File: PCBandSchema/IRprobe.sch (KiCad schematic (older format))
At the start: 16 parts, among them J1 Conn_01x03_Male, Q1 SFH3015FASMALL-FOOTPRINT, U1 ATtiny25-SSU

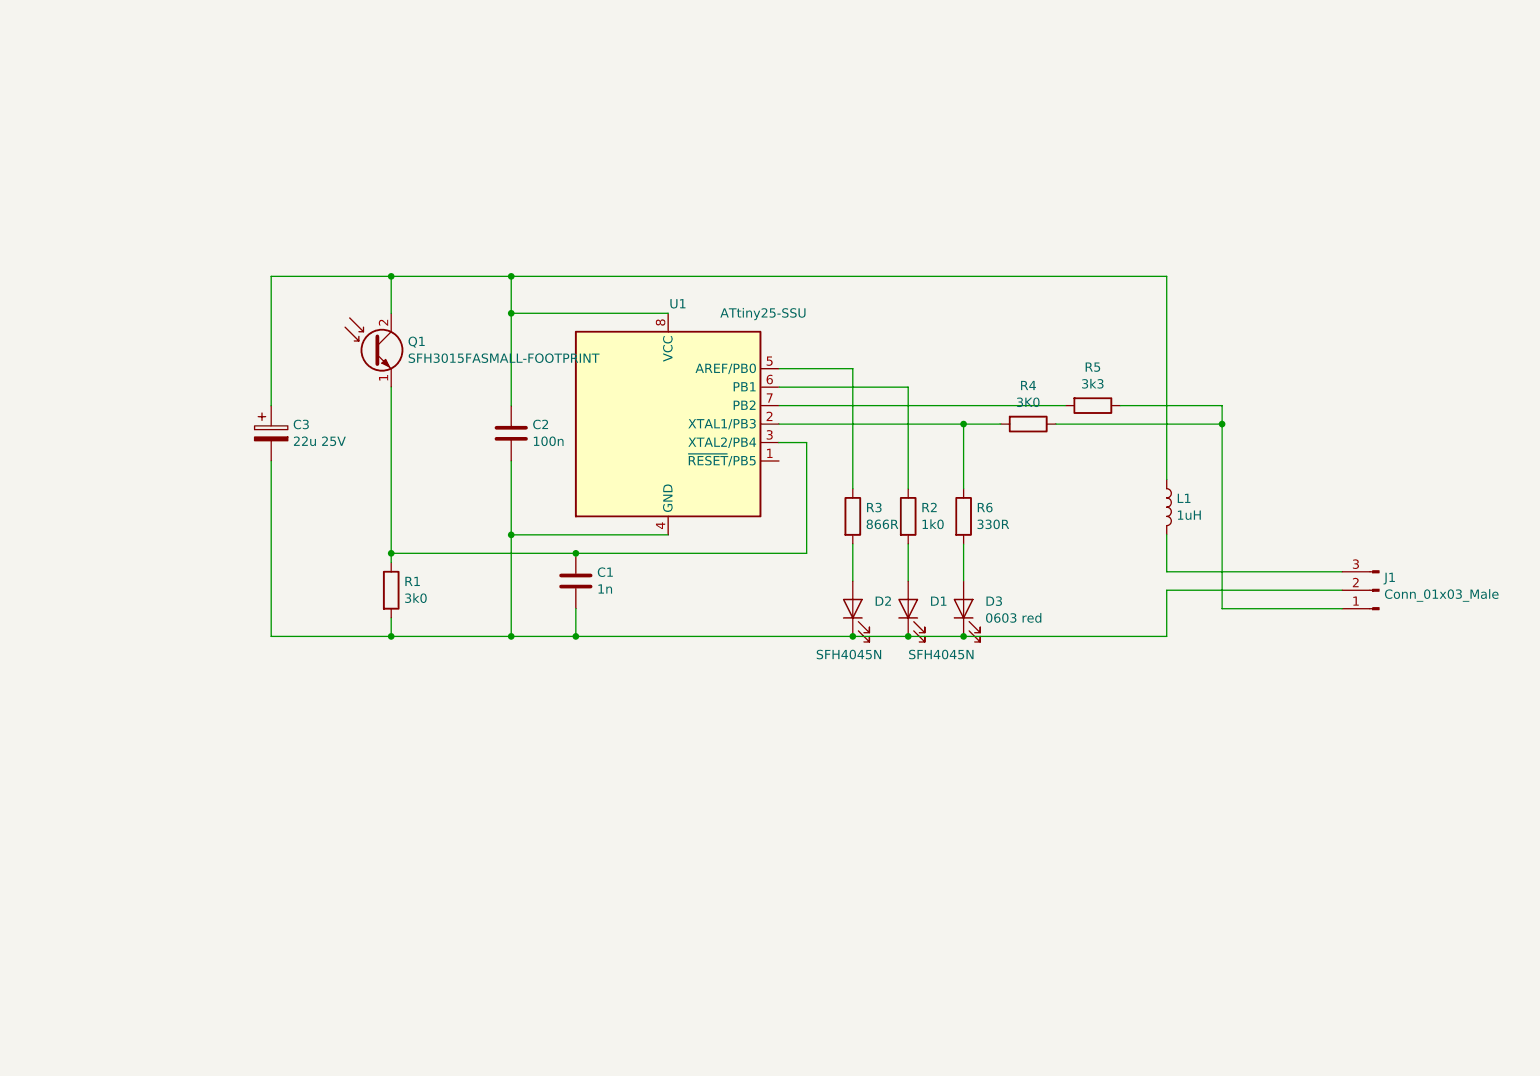
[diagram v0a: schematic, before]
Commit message: Ver 2 Added ADXL
Second version with same footprint but added ADXL on top of IR probe.
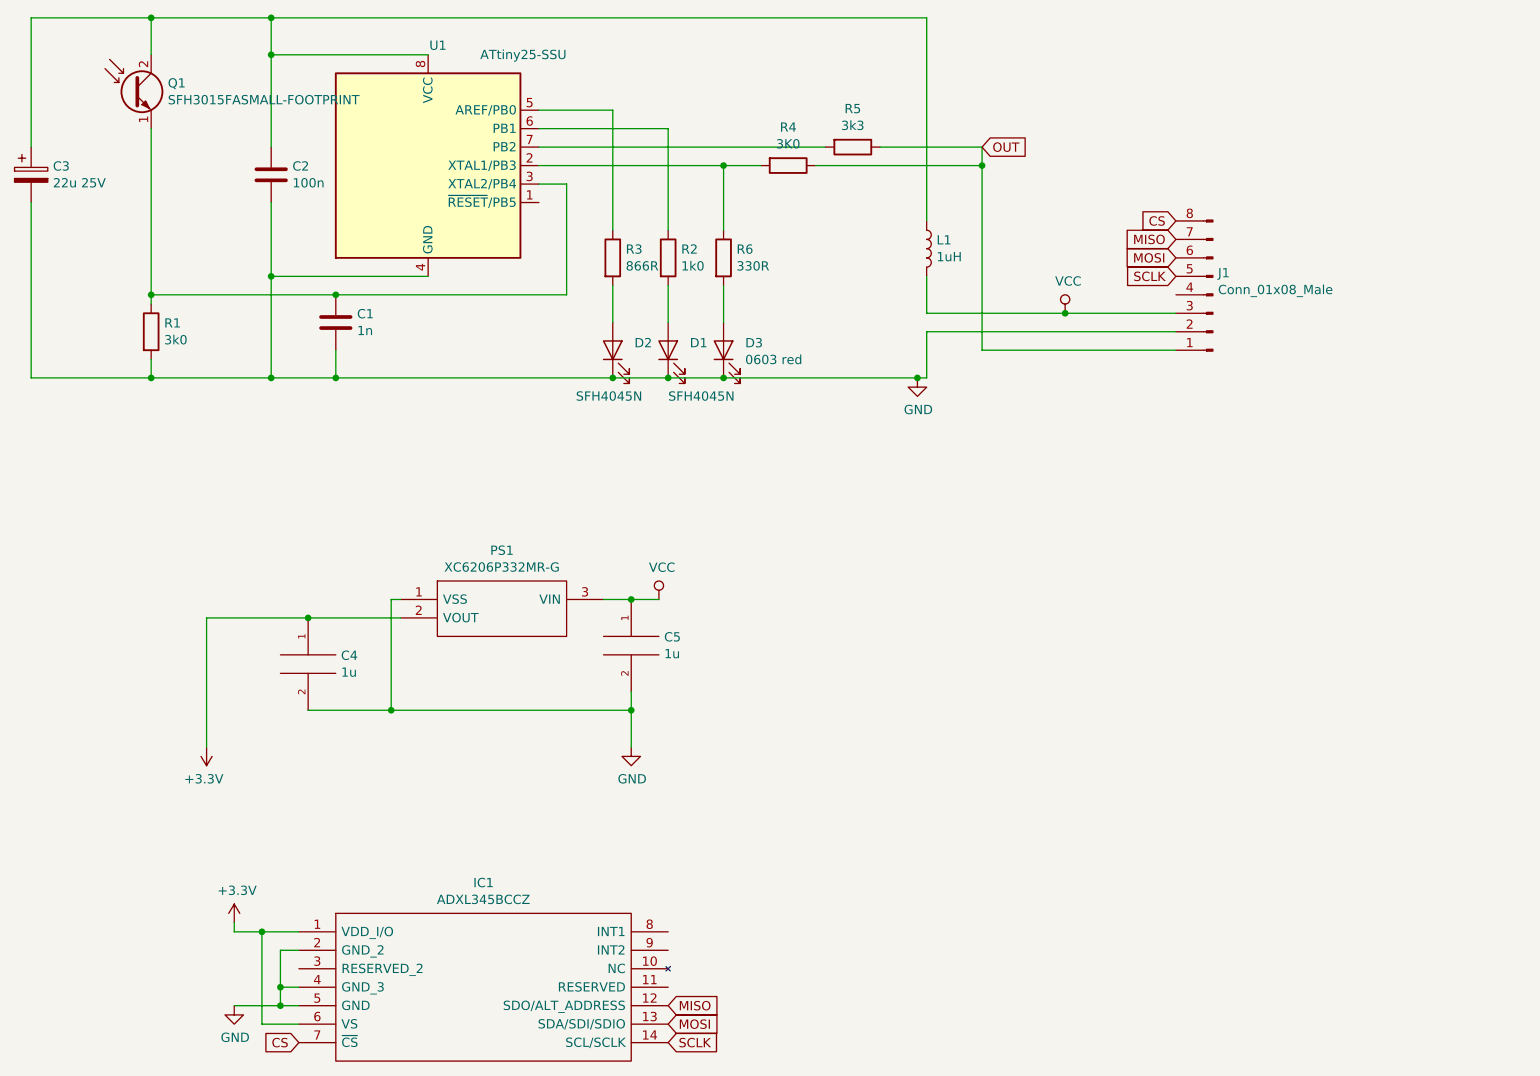
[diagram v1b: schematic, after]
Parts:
- removed J1: Conn_01x03_Male, Connector_PinHeader_2.54mm:PinHeader_1x03_P2.54mm_Horizontal, symbol Connector:Conn_01x03_Male
- added C4, C5: 1u, Capacitor_SMD:C_0603_1608Metric, symbol pspice:C
- added IC1: ADXL345BCCZ, SamacSys_Parts:LGA14R80P3X6_300X500X100, symbol SamacSys_Parts:ADXL345BCCZ
- added J1: Conn_01x08_Male, Connector_PinHeader_2.54mm:PinHeader_2x04_P2.54mm_Vertical, symbol Connector:Conn_01x08_Male
- added PS1: XC6206P332MR-G, SamacSys_Parts:SOT95P280X130-3N, symbol SamacSys_Parts:XC6206P332MR-G
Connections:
- net GND: now reaches C1.2, C2.2, C3.2, D1.1 (K), D2.1 (K), D3.1 (K), R1.2, U1.4 (GND)
- net GND: now also C4.2, C5.2, IC1.2 (GND_2), IC1.4 (GND_3), IC1.5 (GND), J1.2 (Pin_2), PS1.1 (VSS)
- net OUT: now reaches R4.1, R5.1
- net OUT: now also J1.1 (Pin_1)
- net VCC: now reaches L1.2
- net VCC: now also C5.1, J1.3 (Pin_3), PS1.3 (VIN)
- new net +3V3: C4.1, IC1.1 (VDD_I/O), IC1.6 (VS), PS1.2 (VOUT)
- new net CS: IC1.7 (~CS), J1.8 (Pin_8)
- new net MISO: IC1.12 (SDO/ALT_ADDRESS), J1.7 (Pin_7)
- new net MOSI: IC1.13 (SDA/SDI/SDIO), J1.6 (Pin_6)
- new net SCLK: IC1.14 (SCL/SCLK), J1.5 (Pin_5)
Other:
- moved on the sheet: C1, C2, C3, D1, D2, D3, L1, Q1, R1, R2, R3, R4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
